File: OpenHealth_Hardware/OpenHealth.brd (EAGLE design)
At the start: 141 x 162.6 mm, 22 parts

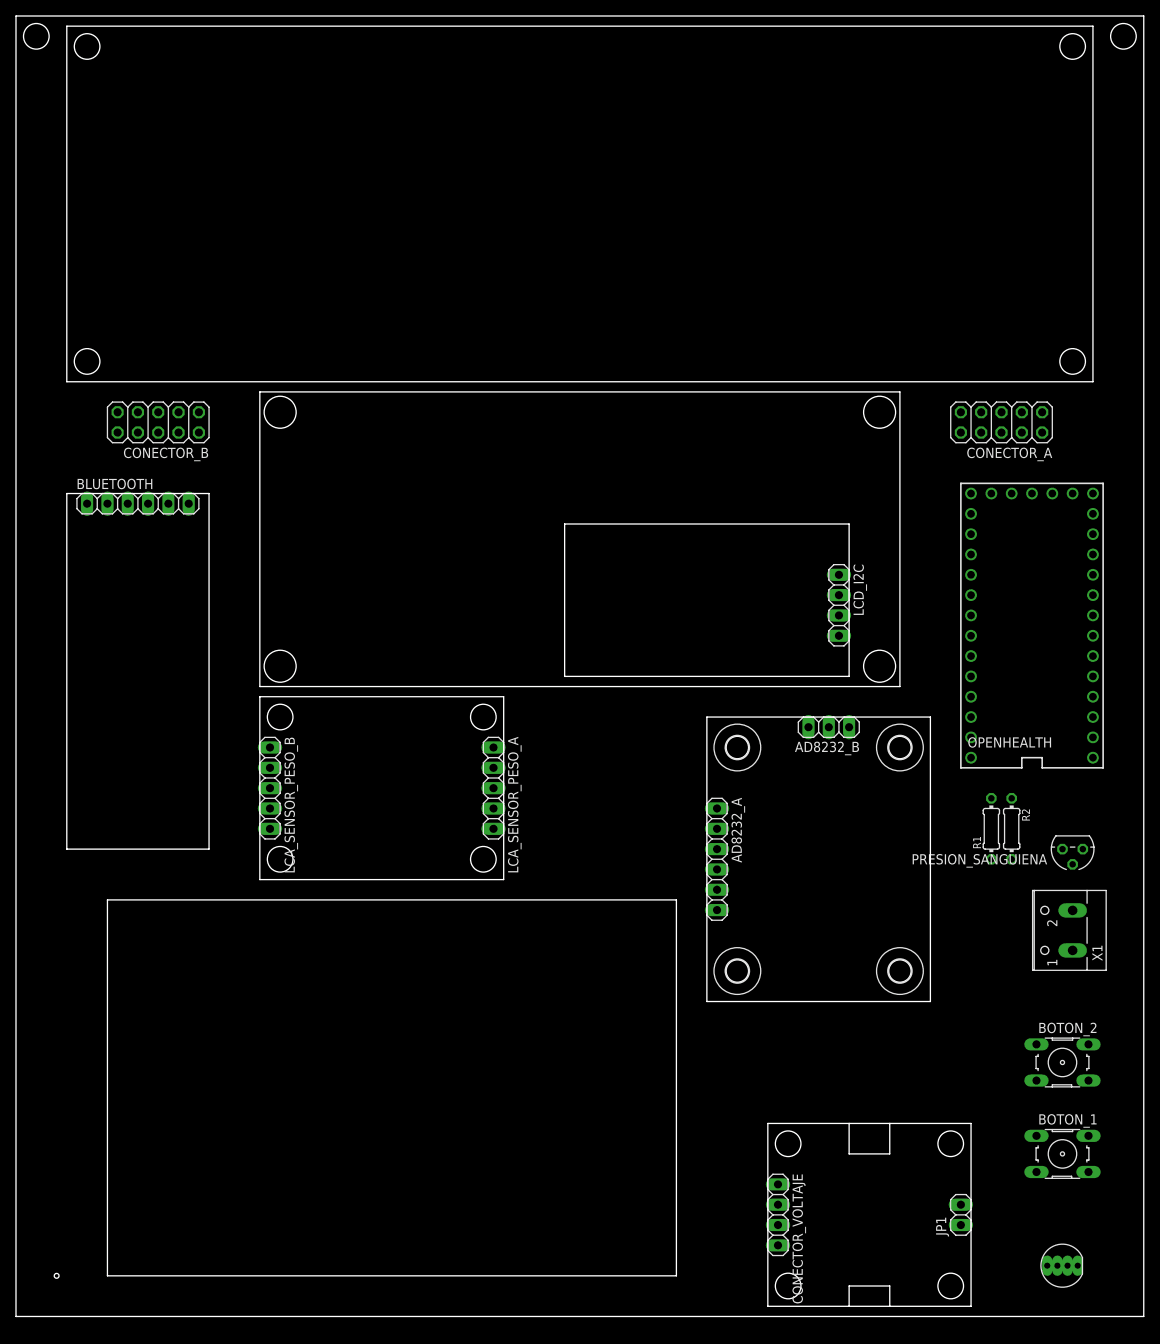
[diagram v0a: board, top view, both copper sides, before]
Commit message: Reduccion de la placa madre, se agrego las resistencias faltantes del led y se ordeno previo al enrutado
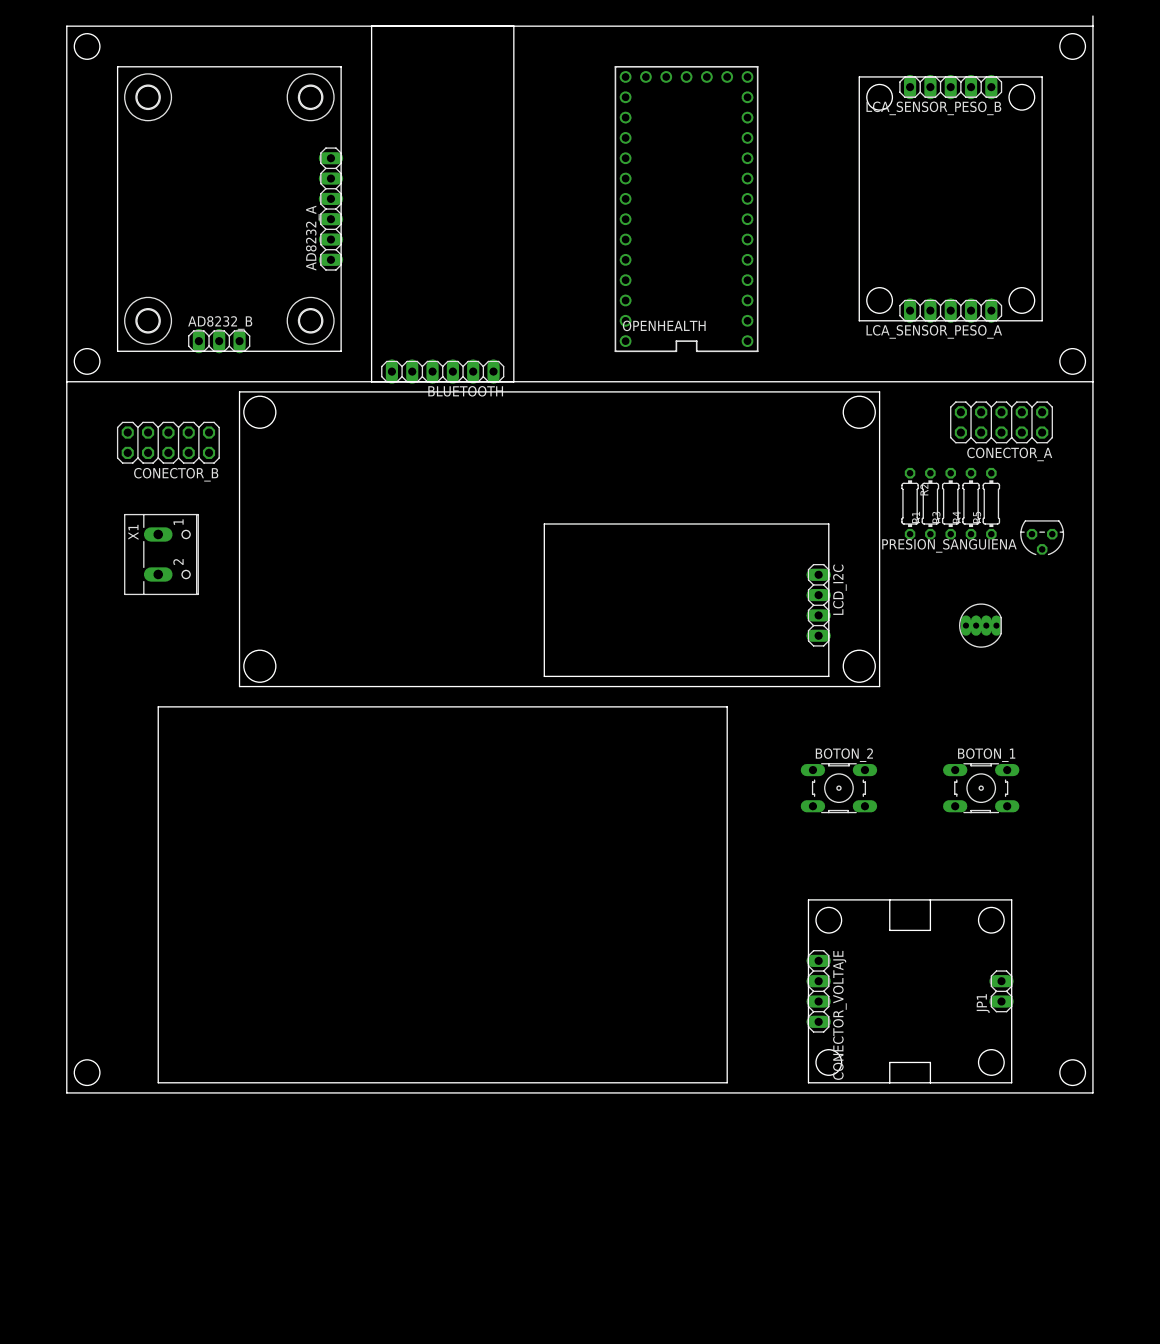
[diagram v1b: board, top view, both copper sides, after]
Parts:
- added R3, R4, R5: 330, resistor:0204/7
- moved U$4 144.1 mm to (-58.4, 144.8), turned to 90 degrees
- moved LCA_SENSOR_PESO_B 122.1 mm to (41.9, 146.1), turned to 180 degrees
- moved U$3 121.5 mm to (-38.1, 144.8), turned to 90 degrees
- moved X1 121.2 mm to (-55.9, 87.6), turned to 270 degrees
- moved U$1 108.1 mm to (-58.4, 116.8), turned to 90 degrees
- moved AD8232_A 94.5 mm to (-35.6, 130.8), turned to 90 degrees
- moved AD8232_B 90.2 mm to (-49.5, 114.3), turned to 0 degrees
- moved LCA_SENSOR_PESO_A 82.6 mm to (41.9, 118.1), turned to 180 degrees
- moved LED_RGB 80.7 mm to (45.7, 78.7)
- moved U$2 75.4 mm to (-38.1, 116.8), turned to 90 degrees
- moved OPENHEALTH 67.6 mm to (8.89, 130.8)
- moved BOTON_1 46.8 mm to (45.7, 58.4)
- moved BOTON_2 44.2 mm to (27.9, 58.4)
- moved R2 42.6 mm to (36.8, 94.0)
- moved BLUETOOTH 41.5 mm to (-21.6, 110.5), turned to 180 degrees
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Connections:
- new net N$2: LED_RGB.4, R3.1
- new net N$3: LED_RGB.1, R5.1
- new net N$4: LED_RGB.3, R4.1
- net PIN_B: now also R3.2; no longer LED_RGB.4
- net PIN_G: now also R4.2; no longer LED_RGB.3
- net PIN_R: now also R5.2; no longer LED_RGB.1
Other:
- board size 141 x 162.6 mm -> 128.3 x 134.6 mm
